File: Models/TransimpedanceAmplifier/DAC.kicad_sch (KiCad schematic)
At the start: 7 parts, among them U10 DAC81401

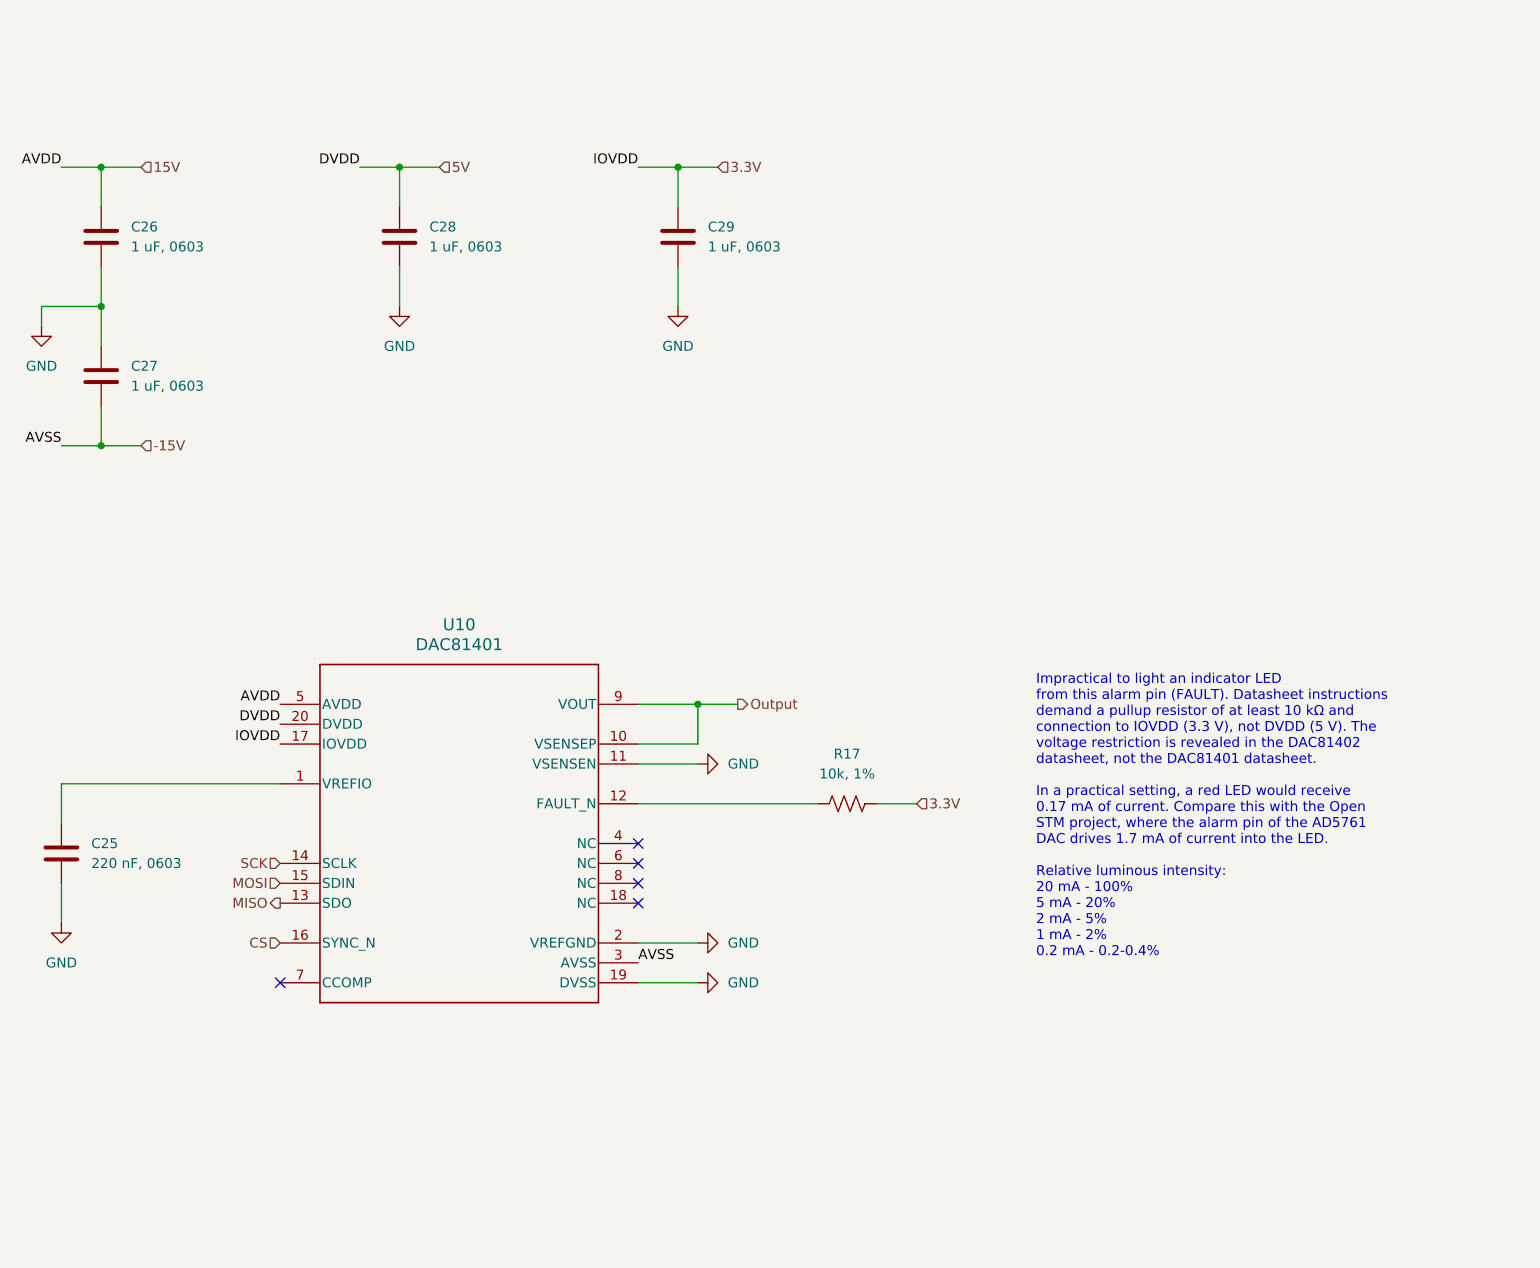
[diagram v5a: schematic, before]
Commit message: Reorganized the DAC decoupling network for ease of modification
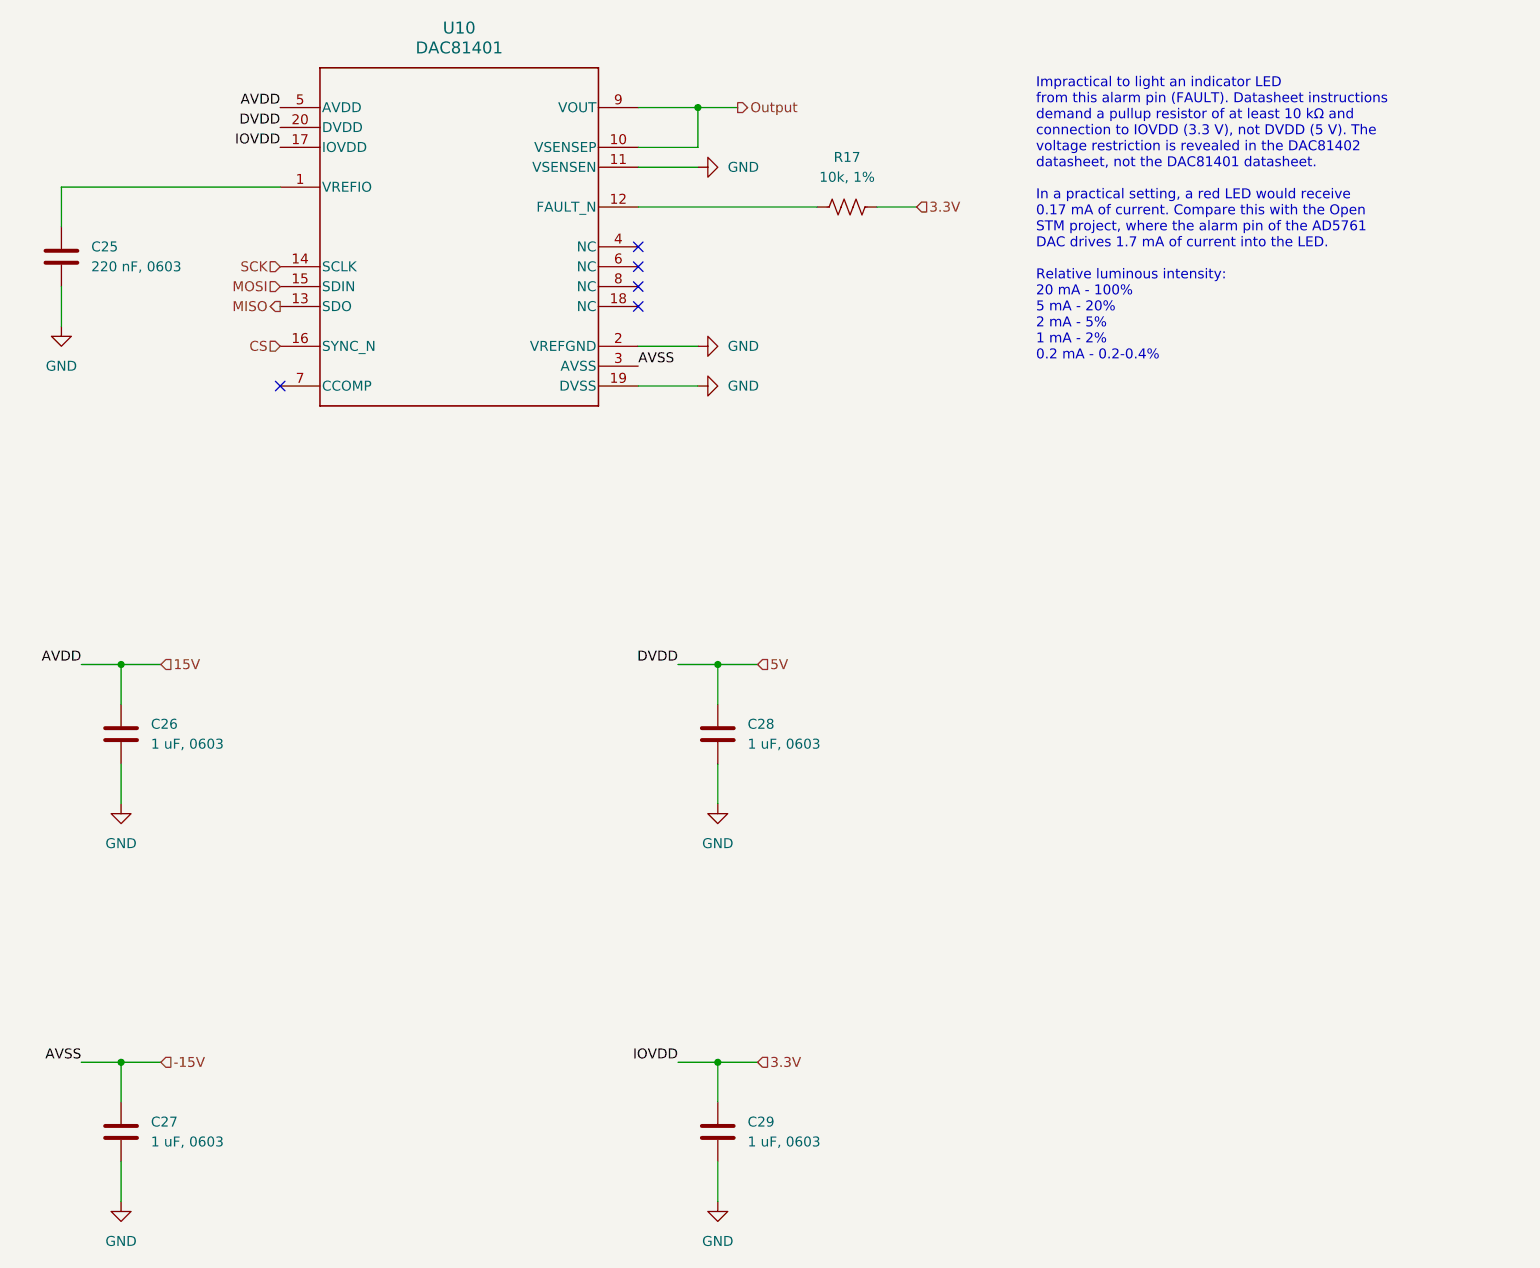
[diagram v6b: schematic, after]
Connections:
- net -15V: now also C27.1; no longer C27.2
- net GND: now also C27.2; no longer C27.1
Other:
- moved on the sheet: C25, C26, C27, C28, C29, R17, U10

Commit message: First successful ERC
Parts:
- added NT1, NT2, NT3, NT4: NetTie_2, symbol Device:NetTie_2
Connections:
- net -15V: now also NT2.2; no longer C27.1, U10.3 (AVSS)
- net 15V: now also NT1.2; no longer C26.1, U10.5 (AVDD)
- net 3.3V: now also NT4.2; no longer C29.1, U10.17 (IOVDD)
- net 5V: now also NT3.2; no longer C28.1, U10.20 (DVDD)
- new net AVDD: C26.1, NT1.1, U10.5 (AVDD)
- new net AVSS: C27.1, NT2.1, U10.3 (AVSS)
- new net DVDD: C28.1, NT3.1, U10.20 (DVDD)
- new net IOVDD: C29.1, NT4.1, U10.17 (IOVDD)
